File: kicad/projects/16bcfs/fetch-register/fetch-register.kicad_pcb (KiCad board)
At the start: 4 copper layers, 86.5 x 43.2 mm, 119 parts, among them J1 InstrRegInput, J2 ALU Bus B, J3 FetchBusInput, J4 Main Bus, J5 Control Signals, J6 Address Bus 2, J7 Power, U1 74HC574, U10 74HC574, U11 74HC574, U12 74HC541, U2 74HC574, U3 74HC574, U4 74HC574, U5 74HC574, U6 74HC574, U7 74HC04, U8 74HC574, U9 74HC574

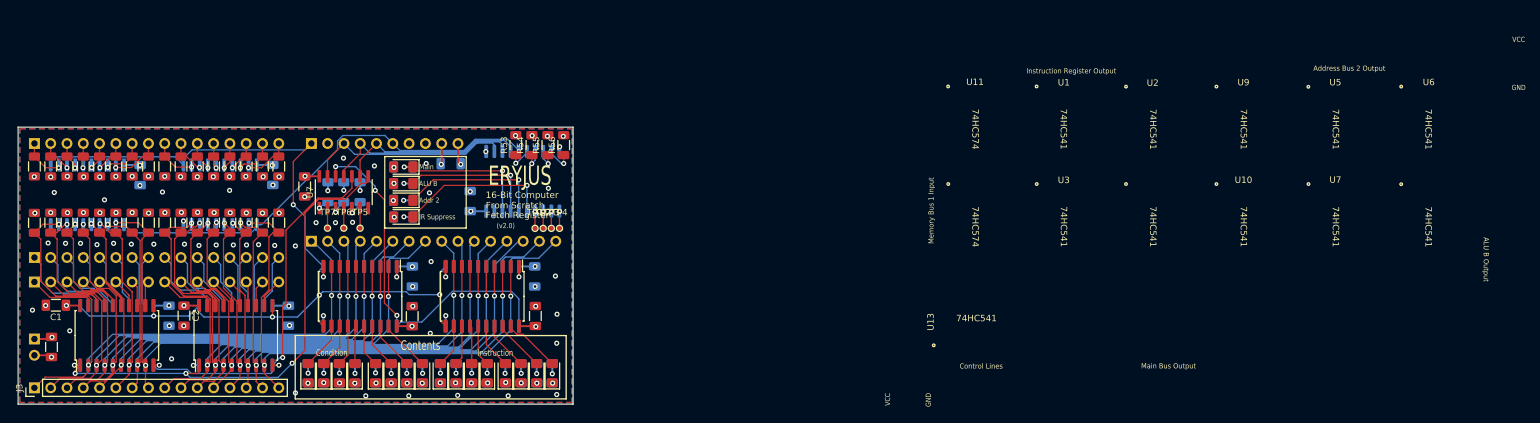
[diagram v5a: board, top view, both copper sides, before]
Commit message: Complete the silkscreen on the Fetch Register
This commit completed the silkscreen for the fetch register.

Overall, this is the completion of the Fetch Register design and PCB
layout.
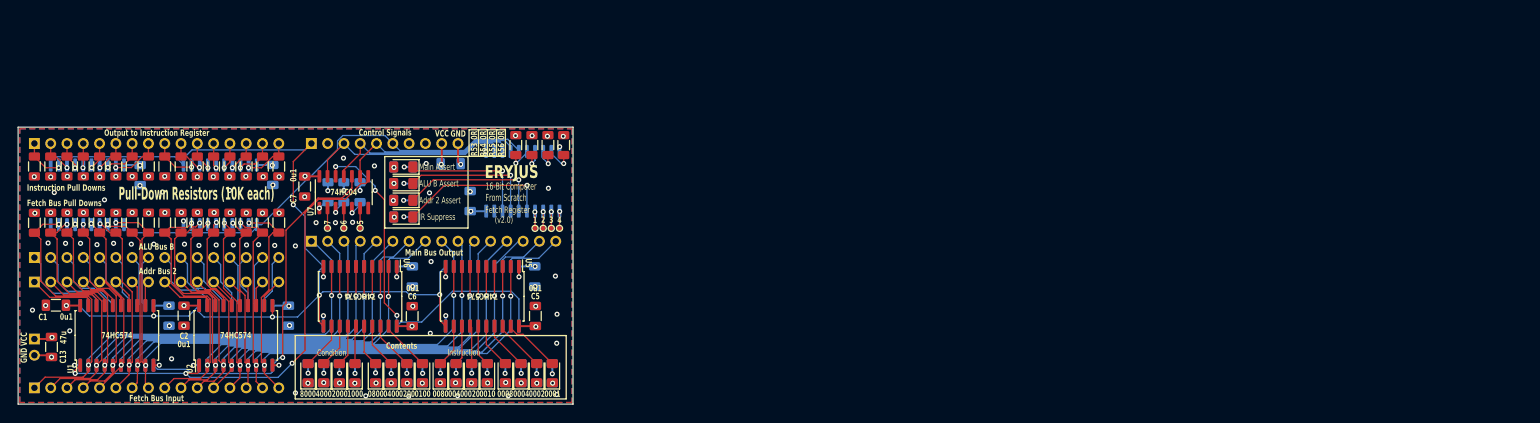
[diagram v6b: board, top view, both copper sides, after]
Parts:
- J3: moved to B.Cu
- turned J3 to -90 degrees
- turned TP3 to -90 degrees
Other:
- board text added: "0001"
- board text added: "0002"
- board text added: "0004"
- board text added: "0008"
- board text added: "0010"
- board text added: "0020"
- board text added: "0040"
- board text added: "0080"
- board text added: "0100"
- board text added: "0200"
- board text added: "0400"
- board text added: "0800"
- board text added: "0R"
- board text added: "0u1"
- board text added: "1"
- board text added: "1000"
- board text added: "1K"
- board text added: "2"
- board text added: "2000"
- board text added: "3"
- board text added: "4"
- board text added: "4000"
- board text added: "47u"
- board text added: "5"
- board text added: "6"
- board text added: "7"
- board text added: "74HC04"
- board text added: "8000"
- board text added: "ALU B Assert"
- board text added: "ALU Bus B"
- board text added: "Addr 2 Assert"
- board text added: "Addr Bus 2"
- board text added: "Control Signals"
- board text added: "Fetch Bus Input"
- board text added: "Fetch Bus Pull Downs"
- board text added: "Instruction Pull Downs"
- board text added: "Main Assert"
- board text added: "Output to Instruction Register"
- board text added: "Pull-Down Resistors (10K each)"
- board text removed: "ALU B"
- board text removed: "ALU B Output"
- board text removed: "Addr 2"
- board text removed: "Address Bus 2 Output"
- board text removed: "Control Lines"
- board text removed: "Instruction Register Output"
- board text removed: "Main"
- board text removed: "Memory Bus 1 Input"
- board text removed: "U1"
- board text removed: "U10"
- board text removed: "U11"
- board text removed: "U13"
- board text removed: "U2"
- board text removed: "U3"
- board text removed: "U5"
- board text removed: "U6"
- board text removed: "U7"
- board text removed: "U9"
